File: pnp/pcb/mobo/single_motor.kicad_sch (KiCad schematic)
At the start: 17 parts, among them J27 TMC_PIN_HEADER, M1 Stepper_Motor

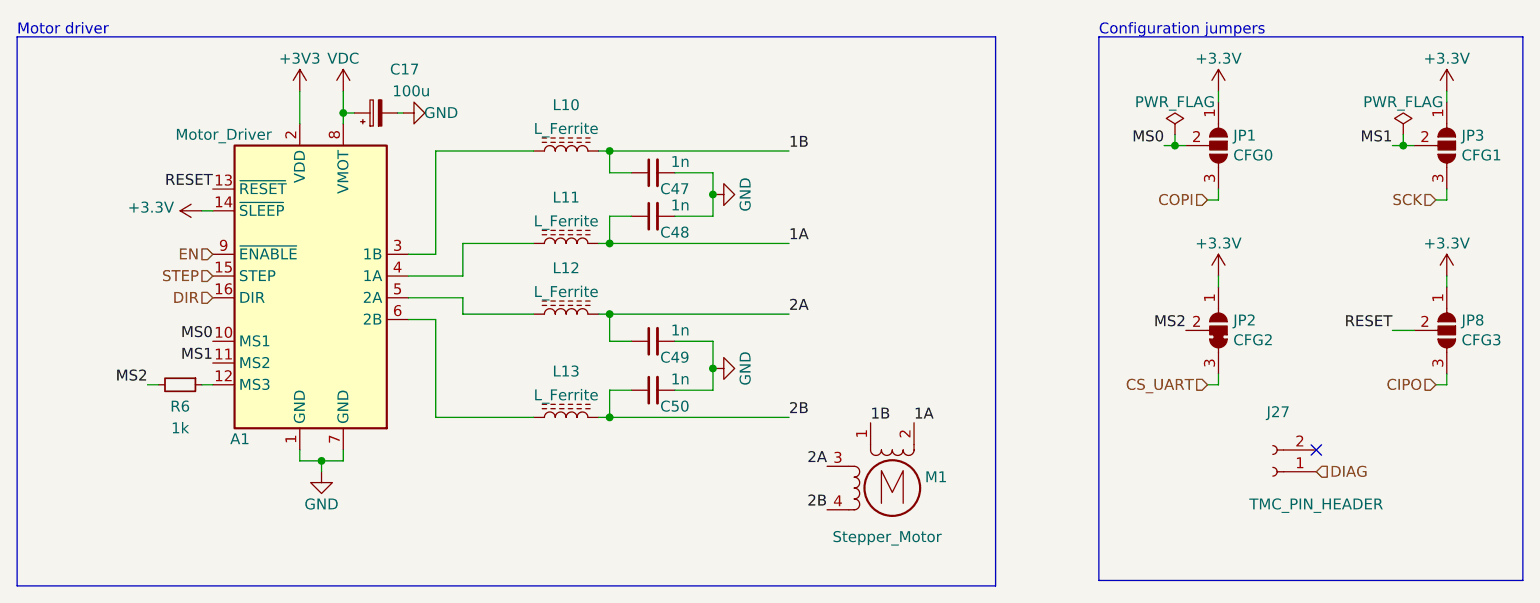
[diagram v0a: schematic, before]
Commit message: tweak PN of mobo
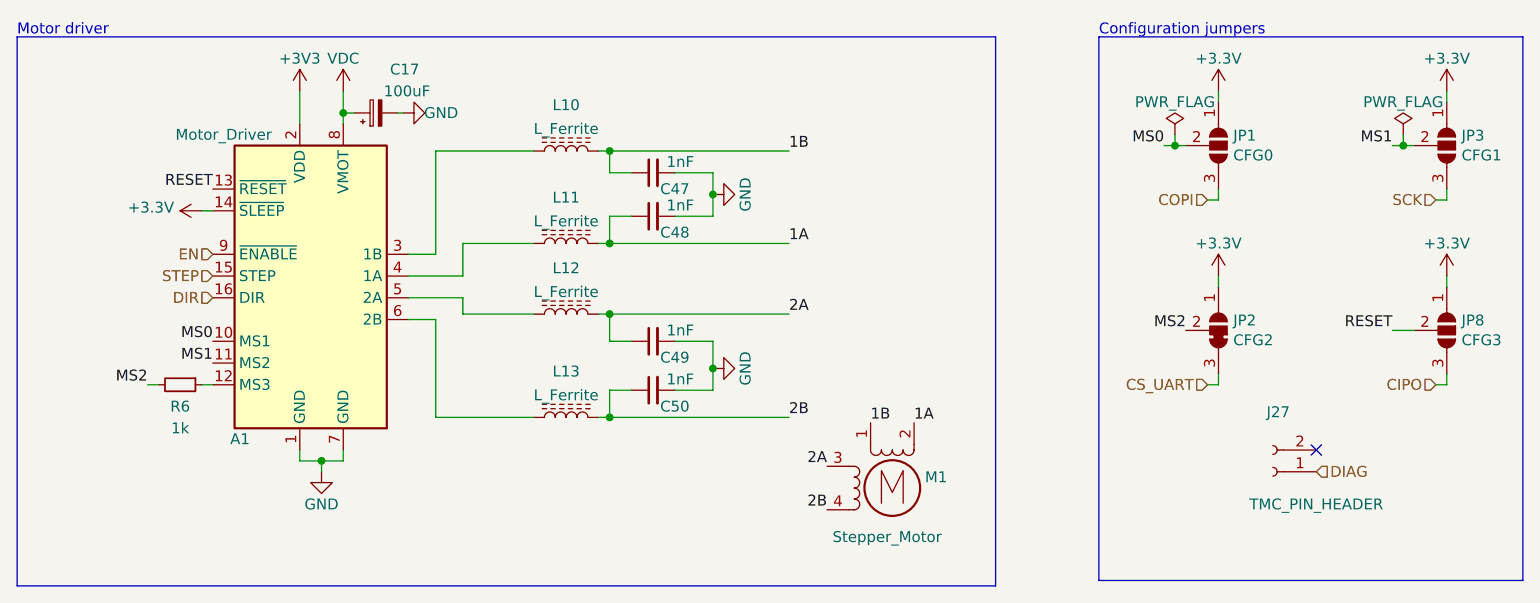
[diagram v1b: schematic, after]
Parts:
- A1: LCSC (none) -> C27438 x2
- C17: value 100u -> 100uF
- C47, C48, C49, C50: value 1n -> 1nF; LCSC (none) -> C94121
- J27: LCSC (none) -> C49661
- JP1, JP2, JP3, JP8: LCSC (none) -> DNP
- L10, L11, L12, L13: LCSC (none) -> C79382
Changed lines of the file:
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@@
+      (effects (font (size 1.27 1.27)) hide)
+    )
+    (property "LCSC" "C79382" (at 105.41 121.92 0)
       (effects (font (size 1.27 1.27)) hide)
     )
@@
       (effects (font (size 1.27 1.27)))
     )
-    (property "Value" "1n" (at 118.745 111.76 90)
+    (property "Value" "1nF" (at 118.745 111.76 90)
       (effects (font (size 1.27 1.27)))
     )
@@
     )
     (property "Notes" "50V/10%" (at 115.57 113.03 0)
+      (effects (font (size 1.27 1.27)) hide)
+    )
+    (property "LCSC" "C94121" (at 115.57 113.03 0)
       (effects (font (size 1.27 1.27)) hide)
     )
@@
     )
     (property "Notes" "BIGTREETECH TMC2209" (at 74.295 105.41 0)
+      (effects (font (size 1.27 1.27)) hide)
+    )
+    (property "LCSC" "C27438 x2" (at 74.295 105.41 0)
       (effects (font (size 1.27 1.27)) hide)
     )
@@
       (effects (font (size 1.27 1.27)))
     )
-    (property "Value" "1n" (at 118.745 117.475 90)
+    (property "Value" "1nF" (at 118.745 117.475 90)
       (effects (font (size 1.27 1.27)))
     )
@@
       (effects (font (size 1.27 1.27)) hide)
     )
+    (property "LCSC" "C94121" (at 115.57 118.745 0)
+      (effects (font (size 1.27 1.27)) hide)
+    )
     (pin "1")
     (pin "2")
@@
       (effects (font (size 1.27 1.27)))
     )
-    (property "Value" "1n" (at 118.745 92.075 90)
+    (property "Value" "1nF" (at 118.745 92.075 90)
       (effects (font (size 1.27 1.27)))
     )
@@
       (effects (font (size 1.27 1.27)) hide)
     )
+    (property "LCSC" "C94121" (at 115.57 93.345 0)
+      (effects (font (size 1.27 1.27)) hide)
+    )
     (pin "1")
     (pin "2")
@@
       (effects (font (size 1.27 1.27)))
     )
-    (property "Value" "1n" (at 118.745 97.155 90)
+    (property "Value" "1nF" (at 118.745 97.155 90)
       (effects (font (size 1.27 1.27)))
     )
@@
       (effects (font (size 1.27 1.27)) hide)
     )
+    (property "LCSC" "C94121" (at 115.57 98.425 0)
+      (effects (font (size 1.27 1.27)) hide)
+    )
     (pin "1")
     (pin "2")
@@
       (effects (font (size 1.27 1.27)) (justify left))
     )
-    (property "Value" "100u" (at 89.535 83.82 90)
+    (property "Value" "100uF" (at 89.535 83.82 90)
       (effects (font (size 1.27 1.27)) (justify left))
     )
@@
     )
     (property "Datasheet" "~" (at 181.61 90.17 0)
+      (effects (font (size 1.27 1.27)) hide)
+    )
+    (property "LCSC" "DNP" (at 181.61 90.17 0)
       (effects (font (size 1.27 1.27)) hide)
     )
@@
       (effects (font (size 1.27 1.27)) hide)
     )
+    (property "LCSC" "C79382" (at 105.41 90.805 0)
+      (effects (font (size 1.27 1.27)) hide)
+    )
     (pin "1")
     (pin "2")
@@
     )
     (property "Datasheet" "~" (at 208.28 111.76 0)
+      (effects (font (size 1.27 1.27)) hide)
+    )
+    (property "LCSC" "DNP" (at 208.28 111.76 0)
       (effects (font (size 1.27 1.27)) hide)
     )
@@
       (effects (font (size 1.27 1.27)) hide)
     )
+    (property "LCSC" "C79382" (at 105.41 101.6 0)
+      (effects (font (size 1.27 1.27)) hide)
+    )
     (pin "1")
     (pin "2")
@@
     )
     (property "Datasheet" "~" (at 181.61 111.76 0)
+      (effects (font (size 1.27 1.27)) hide)
+    )
+    (property "LCSC" "DNP" (at 181.61 111.76 0)
       (effects (font (size 1.27 1.27)) hide)
     )
@@
       (effects (font (size 1.27 1.27)) hide)
     )
+    (property "LCSC" "C79382" (at 105.41 109.855 0)
+      (effects (font (size 1.27 1.27)) hide)
+    )
     (pin "1")
     (pin "2")
@@
       (effects (font (size 1.27 1.27)) hide)
     )
+    (property "LCSC" "DNP" (at 208.28 90.17 0)
+      (effects (font (size 1.27 1.27)) hide)
+    )
     (pin "1")
     (pin "2")
@@
       (effects (font (size 1.27 1.27)) hide)
     )
+    (property "LCSC" "C49661" (at 187.96 128.27 0)
+      (effects (font (size 1.27 1.27)) hide)
+    )
